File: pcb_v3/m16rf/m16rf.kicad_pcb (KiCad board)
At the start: 2 copper layers, 209.5 x 125.1 mm, 55 parts, among them J1 r16_D, J3 r16_A, J4 r16_B, J5 r16_C, J8 bus_rf16_1, J9 bus_rf16_2, U1 74LS125, U10 74LS244, U11 74LS244, U13 74LS02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

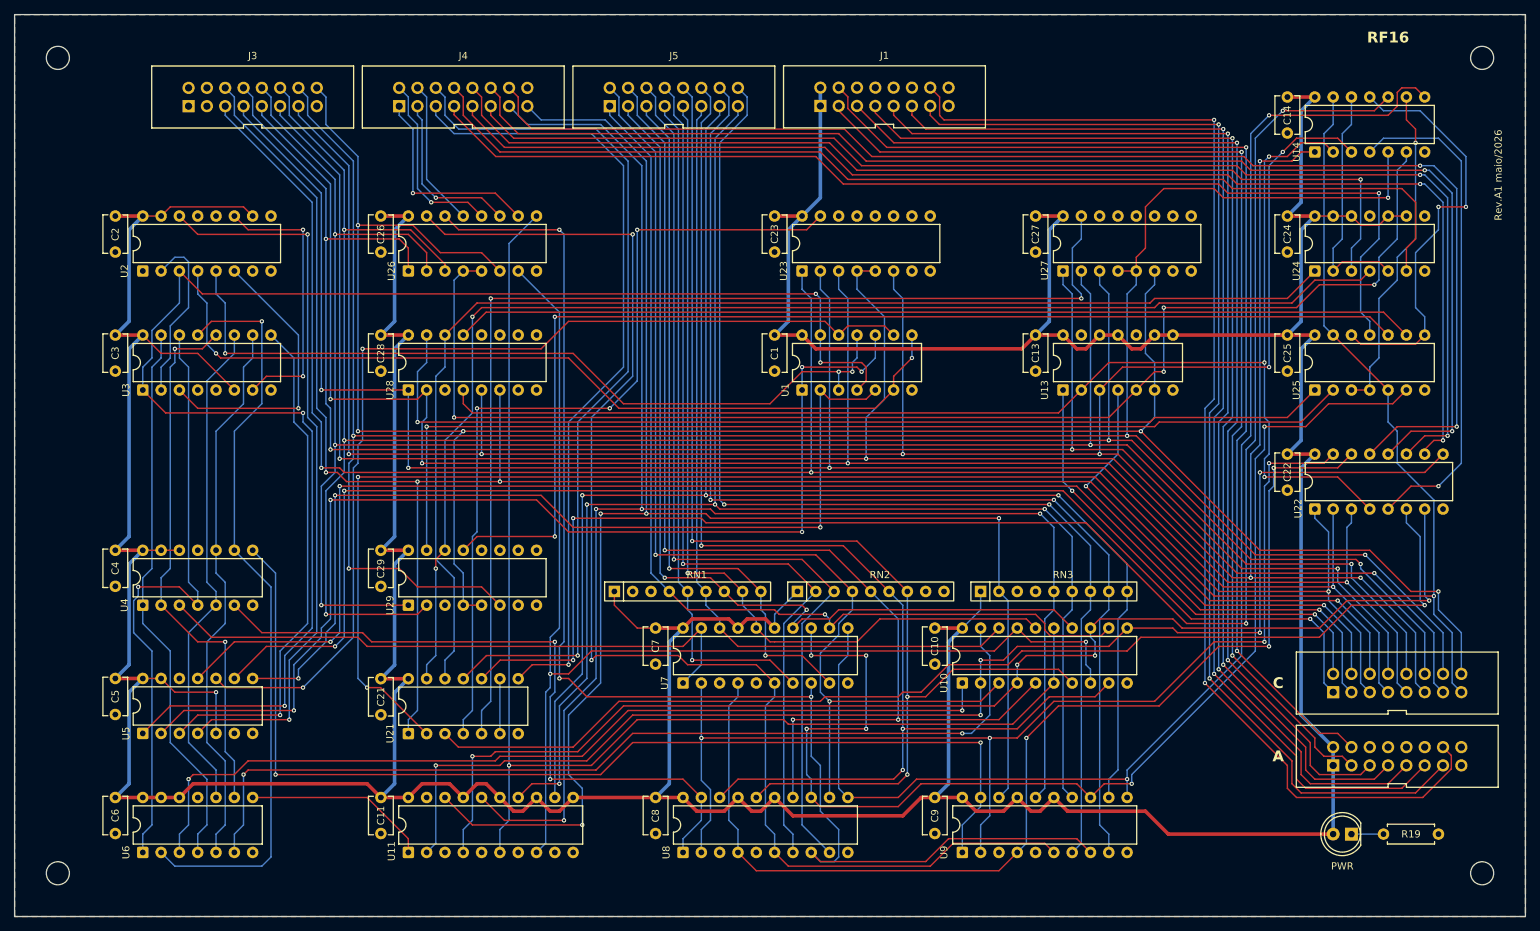
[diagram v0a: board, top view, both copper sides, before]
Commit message: novo layout para pcb v3
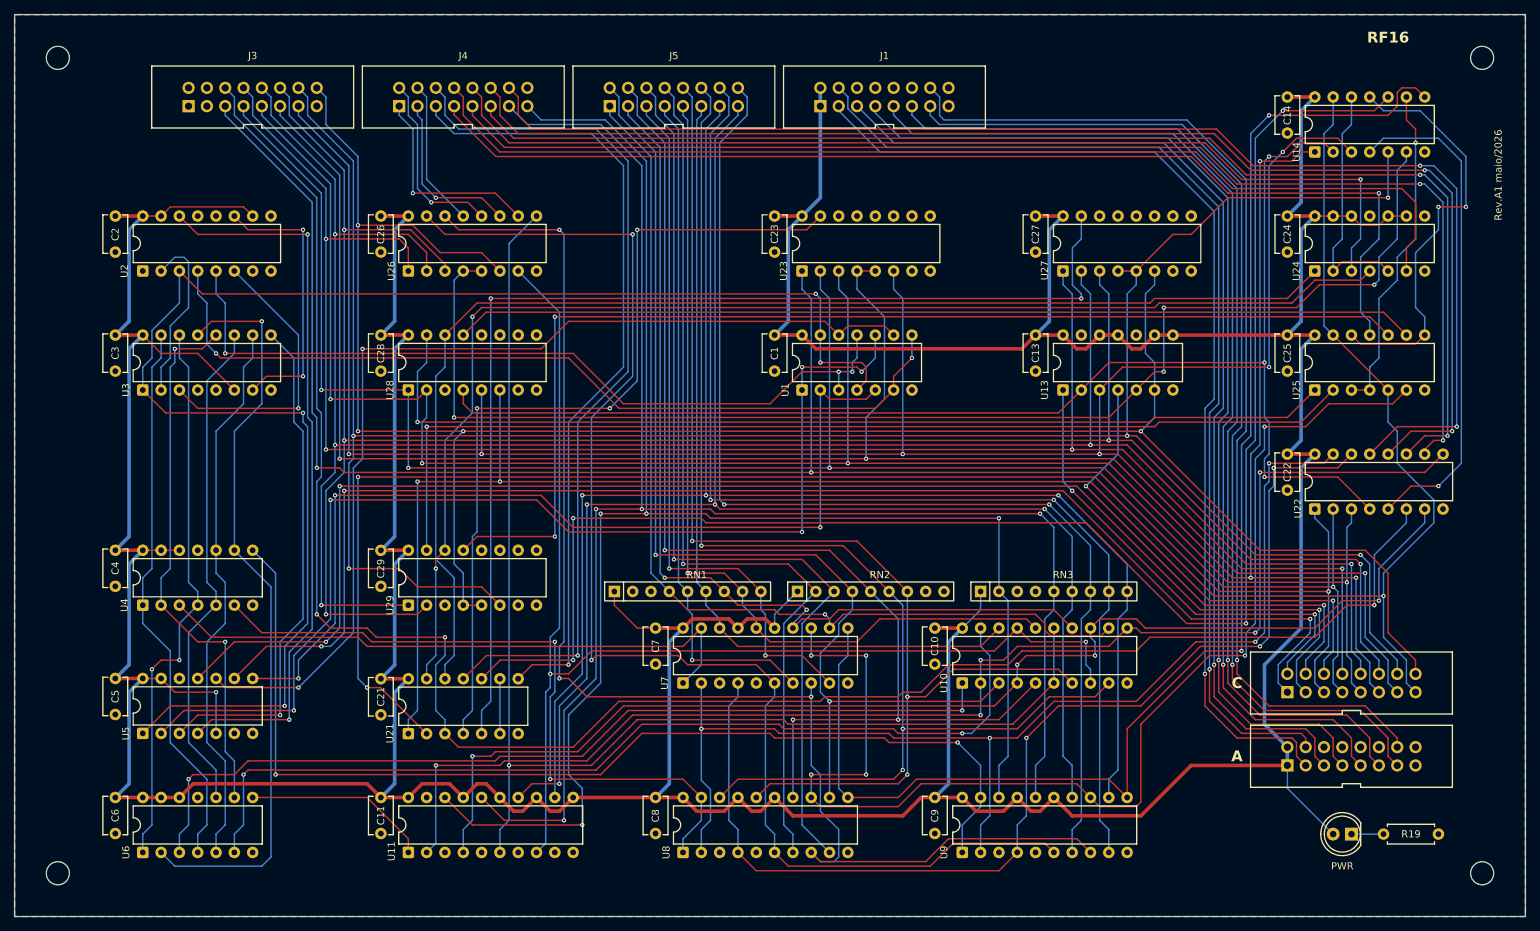
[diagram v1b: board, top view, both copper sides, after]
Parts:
- moved J8 6.35 mm to (213.4, 121.3)
- moved J9 6.35 mm to (213.4, 111.1)
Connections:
- J3 pad 6: wr_enable -> write_clock
- U21 pad 3: write -> write_clock
- U22 pad 6: write -> write_clock
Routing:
- net write_clock: track 0.00 -> 265.3 mm, vias 0 -> 3
- net write: track 159.2 -> 0.00 mm, vias 1 -> 0
- net wr_enable: track 267.0 -> 192.7 mm, vias 4 -> 3
- net data_{7}: track 169.1 -> 146.9 mm, vias 2 -> 1
- net data_{6}: track 161.6 -> 146.9 mm, vias 2 -> 1
- net data_{5}: track 160.3 -> 146.9 mm, vias 2 -> 1
- net data_{4}: track 159.0 -> 146.9 mm, vias 2 -> 1
- net data_{3}: track 157.6 -> 146.7 mm, vias 2 -> 1
- net data_{2}: track 155.7 -> 146.1 mm, vias 2 -> 1
- net swap_1: track 86.5 -> 77.5 mm, vias 1 -> 2
- net rd_addr_3: track 338.2 -> 329.7 mm
- net data_{1}: track 152.9 -> 146.1 mm, vias 2 -> 1
- net data_{0}: track 152.7 -> 146.3 mm, vias 2 -> 1
- net pc_inc: track 166.4 -> 171.7 mm
- net rd_addr_4: track 295.9 -> 290.7 mm, vias 5 -> 4
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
